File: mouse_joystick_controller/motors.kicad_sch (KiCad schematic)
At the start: 0 parts

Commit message: Change brake circuitry again
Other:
- company: (none) -> Howard Hughes Medical Institute
- title: (none) -> mouse_joystick_controller
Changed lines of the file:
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@@
 (kicad_sch (version 20230121) (generator eeschema)
   (paper "A4")
+  (title_block
+    (title "mouse_joystick_controller")
+    (date "2023-06-02")
+    (rev "2.0")
+    (company "Howard Hughes Medical Institute")
+  )
   (wire (pts (xy 189.23 46.99) (xy 186.69 46.99))
     (stroke (width 0) (type default))

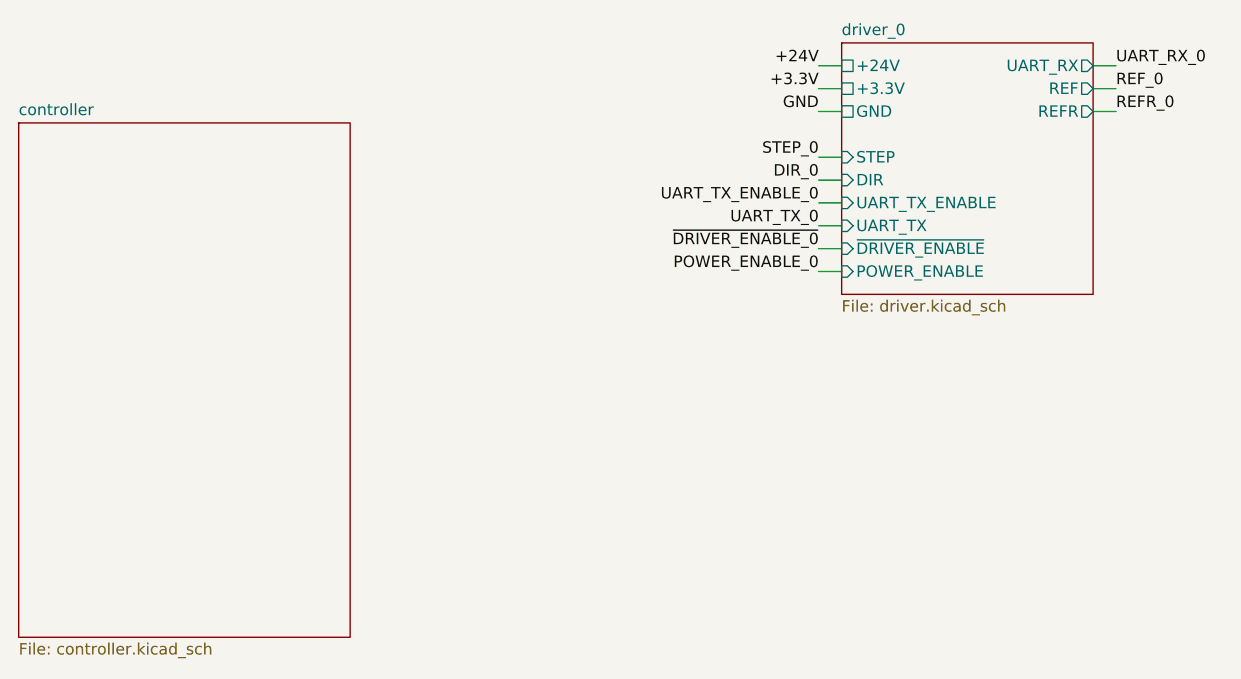
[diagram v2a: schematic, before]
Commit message: power_enable -> standby
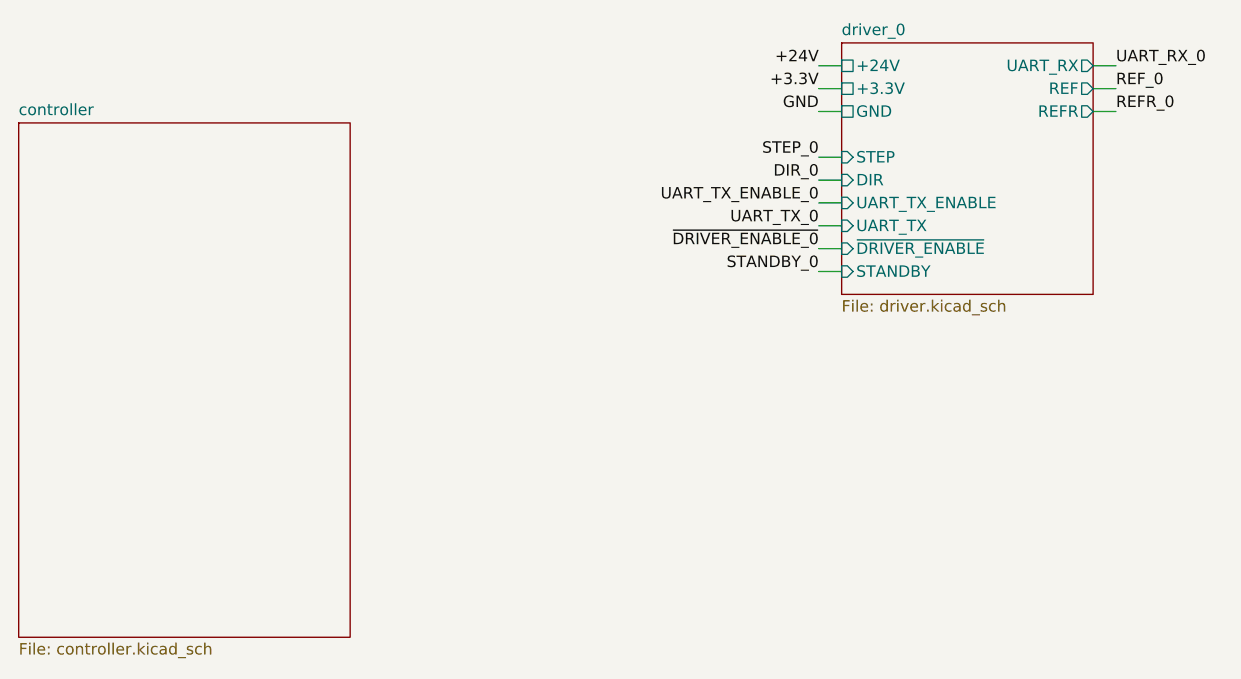
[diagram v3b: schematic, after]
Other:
- sheet driver_0 ports: added STANDBY; removed POWER_ENABLE
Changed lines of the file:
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@@
   (title_block
     (title "mouse_joystick_controller")
-    (date "2023-06-06")
+    (date "2023-06-07")
     (rev "2.0")
     (company "Howard Hughes Medical Institute")
@@
     (effects (font (size 1.27 1.27)) (justify right bottom))
   )
-  (label "POWER_ENABLE_0" (at 186.69 67.31 180) (fields_autoplaced)
+  (label "STANDBY_0" (at 186.69 67.31 180) (fields_autoplaced)
     (effects (font (size 1.27 1.27)) (justify right bottom))
   )
@@
       (effects (font (size 1.27 1.27)) (justify left top))
     )
-    (pin "POWER_ENABLE" input (at 189.23 67.31 180)
+    (pin "STANDBY" input (at 189.23 67.31 180)
       (effects (font (size 1.27 1.27)) (justify left))
     )
